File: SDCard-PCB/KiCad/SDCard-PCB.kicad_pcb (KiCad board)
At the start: 2 copper layers, 80 parts, among them J1 Conn_Coaxial, J10 Conn_01x01, J11 Conn_01x01, J12 Conn_01x01, J13 Conn_01x01, J14 Conn_01x01, J15 Conn_01x08, J16 Conn_01x01, J18 Conn_01x08, J2 Conn_01x01, J3 Conn_01x01, J4 Conn_01x01, J5 Conn_01x01, J6 Conn_01x01, J7 Conn_01x01, J8 Conn_01x01, J9 Conn_01x01, U1 DS90UB933-Q1, U2 TPS62402-Q1, U3 MAX13030EETE+, U4 ATSAME70N21A-CN, Y1 ABM8G-12.000MHZ-4Y-T3

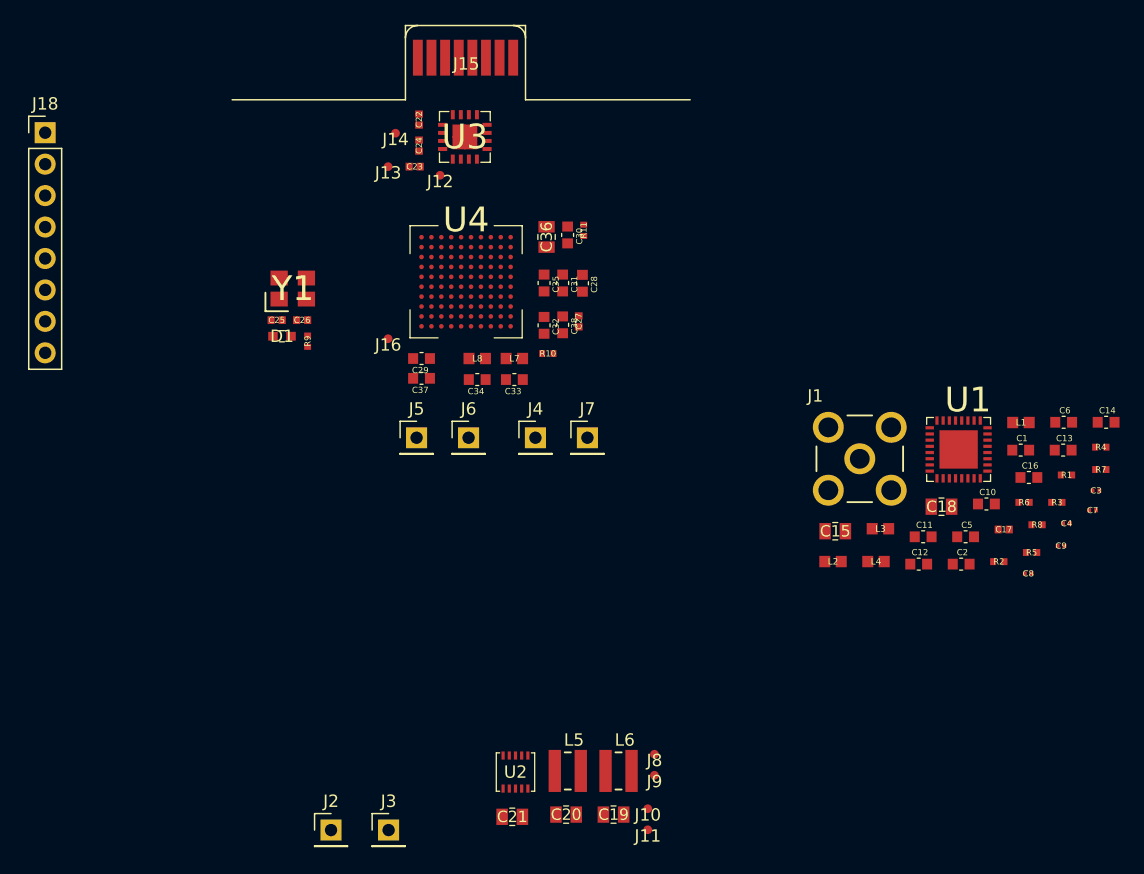
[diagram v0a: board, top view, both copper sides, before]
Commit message: PlugIn PCB PCBNew Progress
More progress in MicroSD PlugIn PCB assembly
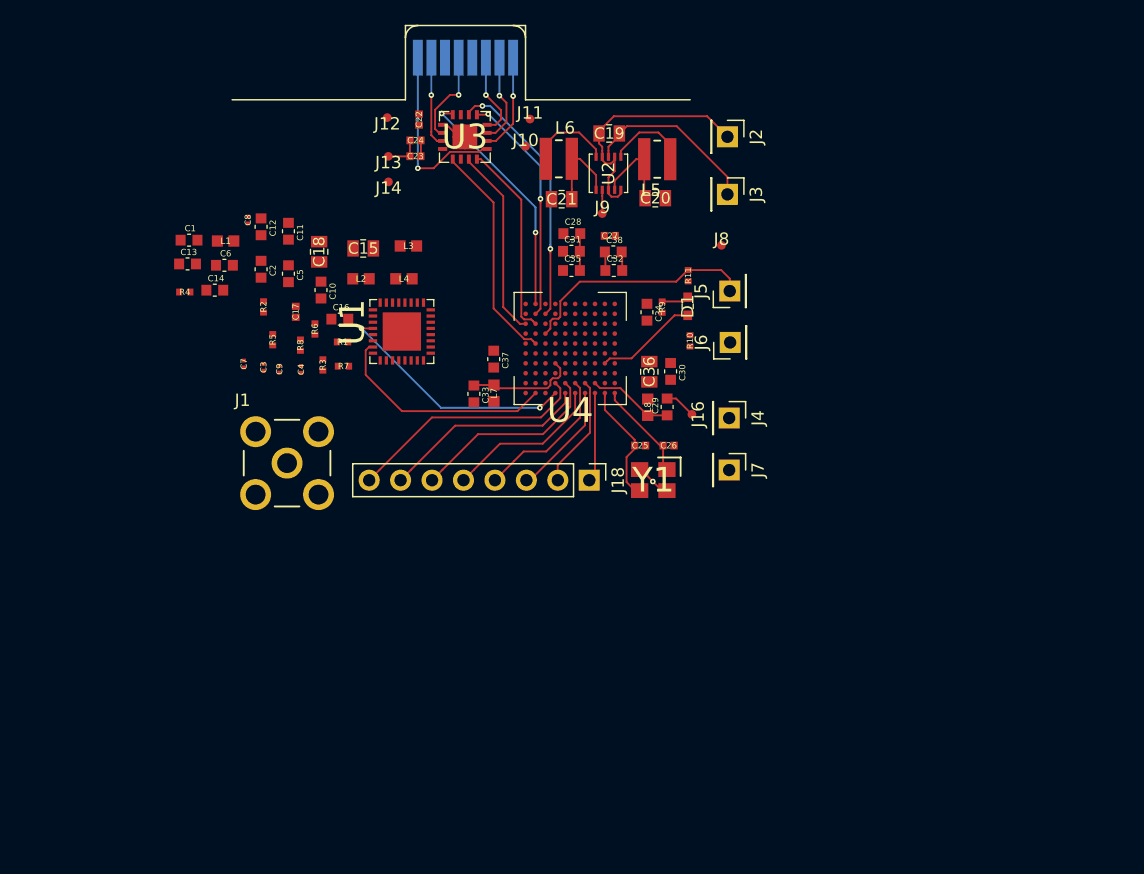
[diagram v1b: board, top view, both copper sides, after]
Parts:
- J15: moved to B.Cu
- moved R4 75.0 mm to (96.2, 68.5)
- moved C14 72.8 mm to (98.6, 68.4)
- moved C13 72.3 mm to (96.4, 66.3)
- moved C7 69.6 mm to (101.0, 74.3), turned to 270 degrees
- moved C1 69.3 mm to (96.5, 64.3)
- moved C8 69.2 mm to (101.3, 62.7), turned to 270 degrees
- moved C6 69.0 mm to (99.4, 66.4)
- moved C3 68.0 mm to (102.5, 74.6), turned to 270 degrees
- moved L1 65.9 mm to (99.5, 64.4)
- moved C9 64.7 mm to (103.8, 74.8), turned to 270 degrees
- moved J2 64.5 mm to (140.0, 56.0), turned to 270 degrees
- moved R5 63.7 mm to (103.3, 72.4), turned to 270 degrees
- moved C4 63.1 mm to (105.6, 74.8), turned to 270 degrees
- moved R2 62.9 mm to (102.5, 69.7), turned to 270 degrees
- moved R7 61.7 mm to (109.0, 74.5)
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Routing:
- net Earth: track 0.00 -> 32.1 mm, vias 0 -> 1
- net /SD_Input/SDCardCMDA: track 0.00 -> 21.1 mm, vias 0 -> 2
- net +BATT: track 0.00 -> 20.2 mm
- net /OnBoardMCU/SD_out1: track 0.00 -> 19.7 mm, vias 0 -> 2
- net /OnBoardMCU/test8: track 0.00 -> 19.6 mm
- net /SD_Input/SDCardCLKA: track 0.00 -> 19.5 mm, vias 0 -> 2
- net /Connectors/SWDIO-Rec: track 0.00 -> 19.4 mm
- net /OnBoardMCU/SD_in3: track 0.00 -> 19.0 mm, vias 0 -> 2
- net /OnBoardMCU/SD_CMD: track 0.00 -> 18.2 mm
- net /OnBoardMCU/SD_in0: track 0.00 -> 18.0 mm
- net /OnBoardMCU/test7: track 0.00 -> 16.7 mm
- net /OnBoardMCU/SD_in2: track 0.00 -> 15.8 mm
- net /OnBoardMCU/test6: track 0.00 -> 15.7 mm
- net /OnBoardMCU/SD_in1: track 0.00 -> 15.5 mm
- net /SD_Input/DAT1: track 0.00 -> 15.2 mm, vias 0 -> 1
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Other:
- copper layers 2 -> 6
- net class Default: clearance 0.2 -> 0.0889; trace_width 0.25 -> 0.0889; via_dia 0.8 -> 0.45; via_drill 0.4 -> 0.2
- rule pad_to_mask_clearance: 0.051 -> 0.0254
- rule trace_clearance: 0.2 -> 0.0889
- rule trace_min: 0.2 -> 0.0889
- rule via_min_drill: 0.3 -> 0.2
- rule via_min_size: 0.4 -> 0.45

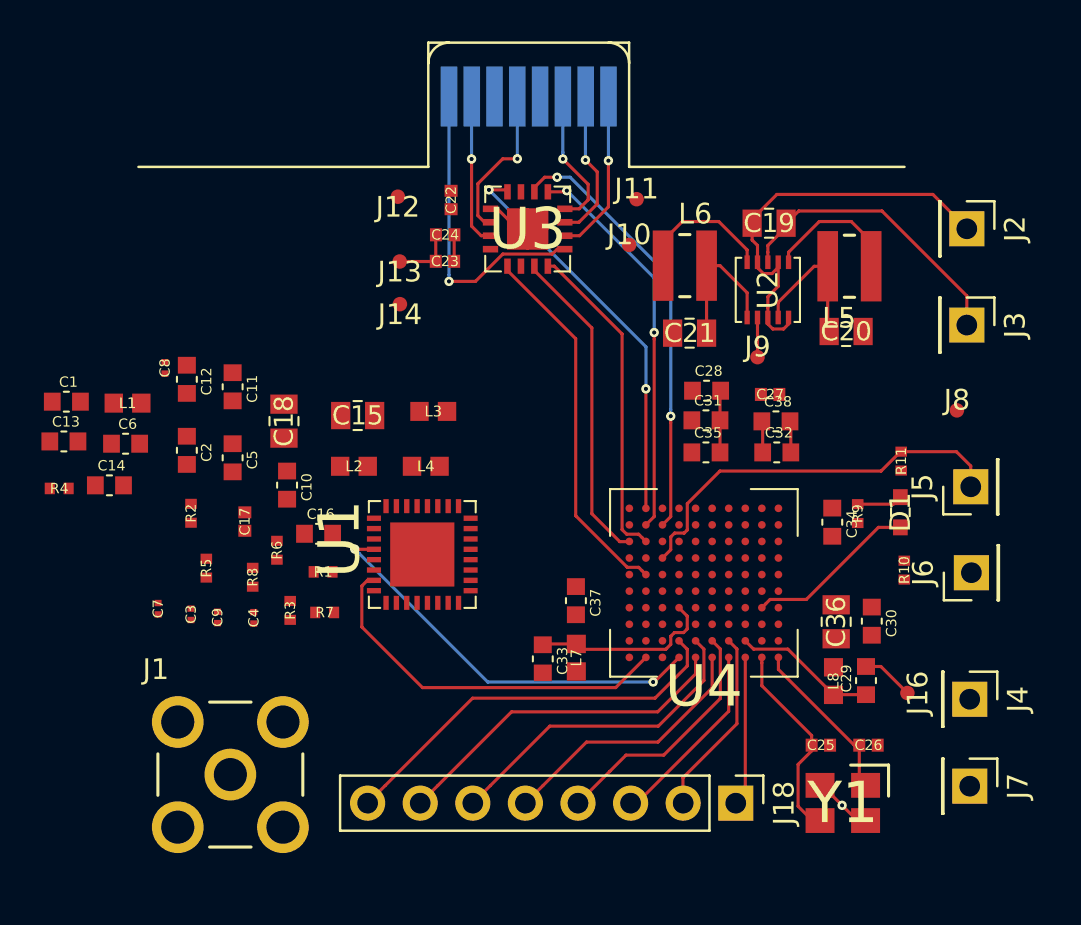
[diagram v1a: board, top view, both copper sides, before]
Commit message: PlugIn PCB Ready
1. Completes the PCBNew drawing for MicroSD PlugIn PCB
2. Passes the DRC rule check
3. Generate Gerber files
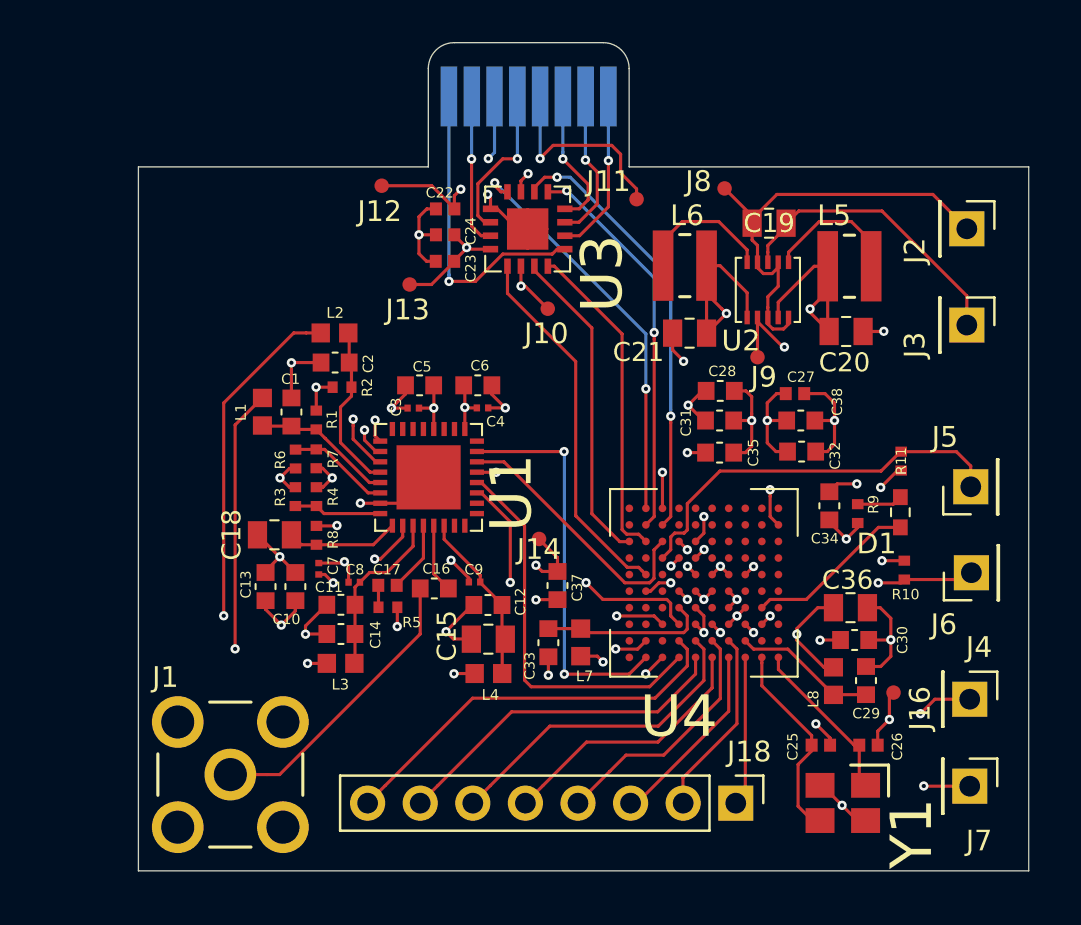
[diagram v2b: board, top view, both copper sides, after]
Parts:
- moved C12 18.2 mm to (116.9, 74.2), turned to 180 degrees
- moved C6 17.2 mm to (116.4, 63.5)
- moved J8 15.5 mm to (128.3, 54.0)
- moved C4 15.0 mm to (116.6, 64.6), turned to 0 degrees
- moved C3 14.6 mm to (113.3, 64.7), turned to 180 degrees
- moved C8 13.8 mm to (110.4, 73.1), turned to 180 degrees
- moved C14 13.3 mm to (109.8, 75.6), turned to 180 degrees
- moved J14 13.2 mm to (119.3, 71.0)
- moved L3 13.0 mm to (109.8, 77.0), turned to 180 degrees
- moved C9 12.5 mm to (116.2, 73.0), turned to 180 degrees
- moved C15 12.5 mm to (116.9, 75.8), turned to 180 degrees
- moved R4 12.4 mm to (108.6, 68.9), turned to 90 degrees
- moved C13 12.0 mm to (106.1, 73.3), turned to 90 degrees
- moved C11 11.8 mm to (109.8, 74.2), turned to 180 degrees
- moved C1 10.9 mm to (107.4, 64.8), turned to 90 degrees
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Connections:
- J14 pad 1: /SD_Input/DAT0 -> +1V2
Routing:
- net Earth: track 32.1 -> 102.2 mm, vias 1 -> 33
- net +1V8: track 8.54 -> 51.3 mm, vias 0 -> 23
- net /OnBoardMCU/SCL: track 0.00 -> 37.7 mm, vias 0 -> 2
- net /OnBoardMCU/SDA: track 0.00 -> 32.7 mm, vias 0 -> 2
- net /OnBoardMCU/LINE_VALID: track 0.00 -> 23.5 mm, vias 0 -> 2
- net /OnBoardMCU/SD_CLK: track 0.00 -> 22.8 mm, vias 0 -> 2
- net /OnBoardMCU/FRAME_VALID: track 0.00 -> 21.1 mm, vias 0 -> 2
- net +3V3: track 9.99 -> 30.2 mm, vias 0 -> 5
- net /Connectors/SWDCLK-Rec: track 0.00 -> 16.1 mm, vias 0 -> 2
- net +1V2: track 0.00 -> 14.8 mm, vias 0 -> 8
- net /OnBoardMCU/SD_out0: track 0.00 -> 14.5 mm, vias 0 -> 2
- net Net-(C16-Pad1): track 0.00 -> 14.2 mm
- net /OnBoardMCU/SD_out3: track 0.00 -> 13.0 mm
- net /OnBoardMCU/SD_out2: track 0.00 -> 10.7 mm, vias 0 -> 2
- net Net-(C12-Pad1): track 0.00 -> 8.43 mm
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- added copper zone on In3.Cu, net +1V2
- added copper zone on In4.Cu, net +1V8
- added copper zone on In3.Cu, net +3V3
- added copper zone on In1.Cu, net Earth
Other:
- board outline added: 43 x 40 mm
- rule trace_min: 0.0889 -> 0.0762
- rule via_min_drill: 0.2 -> 0.1016
- rule via_min_size: 0.45 -> 0.254
